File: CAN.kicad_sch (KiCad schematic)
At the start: 7 parts, among them J10 CAN, U6 LTC2875-DD

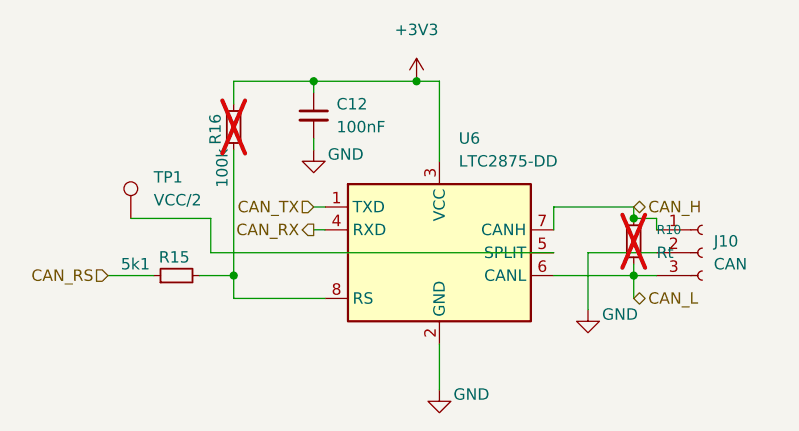
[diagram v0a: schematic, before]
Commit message: feat: more routing
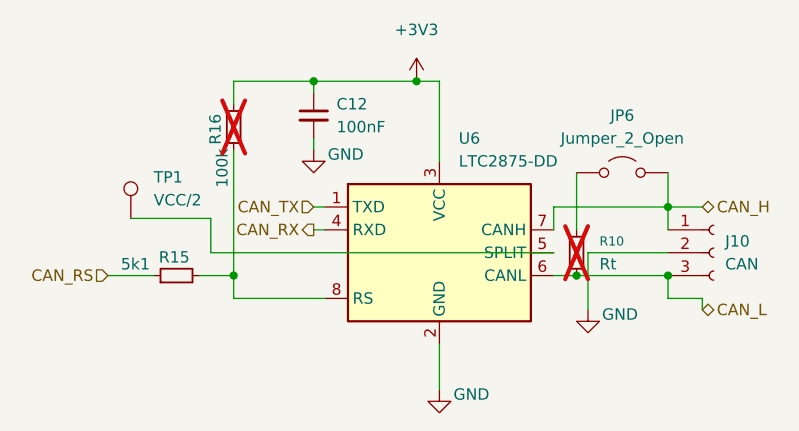
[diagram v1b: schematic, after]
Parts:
- added JP6: Jumper_2_Open, Connector_PinHeader_2.54mm:PinHeader_1x02_P2.54mm_Vertical, symbol Jumper:Jumper_2_Open
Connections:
- net CAN_H: now also JP6.2 (B); no longer R10.1
- new net: JP6.1 (A), R10.1
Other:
- moved on the sheet: J10, R10
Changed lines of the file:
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@@
 	)
 	(junction
-		(at 167.64 95.25)
+		(at 161.29 101.6)
+		(diameter 0)
+		(color 0 0 0 0)
+	)
+	(junction
+		(at 171.45 93.98)
 		(diameter 0)
 		(color 0 0 0 0)
@@
 	)
 	(junction
-		(at 167.64 101.6)
+		(at 171.45 101.6)
 		(diameter 0)
 		(color 0 0 0 0)
@@
 	(wire
 		(pts
+			(xy 171.45 93.98) (xy 175.26 93.98)
+		)
+		(stroke
+			(width 0)
+			(type default)
+		)
+	)
+	(wire
+		(pts
 			(xy 146.05 80.01) (xy 146.05 88.9)
 		)
@@
 	(wire
 		(pts
-			(xy 167.64 95.25) (xy 170.18 95.25)
+			(xy 158.75 93.98) (xy 171.45 93.98)
+		)
+		(stroke
+			(width 0)
+			(type default)
+		)
+	)
+	(wire
+		(pts
+			(xy 161.29 90.17) (xy 161.29 96.52)
 		)
 		(stroke
@@
 	(wire
 		(pts
-			(xy 167.64 101.6) (xy 170.18 101.6)
+			(xy 171.45 90.17) (xy 171.45 93.98)
 		)
 		(stroke
@@
 	(wire
 		(pts
-			(xy 158.75 101.6) (xy 167.64 101.6)
+			(xy 158.75 101.6) (xy 161.29 101.6)
 		)
 		(stroke
@@
 	(wire
 		(pts
+			(xy 175.26 104.14) (xy 171.45 104.14)
+		)
+		(stroke
+			(width 0)
+			(type default)
+		)
+	)
+	(wire
+		(pts
 			(xy 120.65 99.06) (xy 120.65 95.25)
 		)
@@
 	(wire
 		(pts
-			(xy 167.64 93.98) (xy 158.75 93.98)
-		)
-		(stroke
-			(width 0)
-			(type default)
-		)
-	)
-	(wire
-		(pts
-			(xy 167.64 93.98) (xy 167.64 95.25)
+			(xy 171.45 104.14) (xy 171.45 101.6)
 		)
 		(stroke
@@
 	(wire
 		(pts
-			(xy 170.18 99.06) (xy 162.56 99.06)
-		)
-		(stroke
-			(width 0)
-			(type default)
-		)
-	)
-	(wire
-		(pts
-			(xy 170.18 95.25) (xy 170.18 96.52)
+			(xy 171.45 99.06) (xy 162.56 99.06)
+		)
+		(stroke
+			(width 0)
+			(type default)
+		)
+	)
+	(wire
+		(pts
+			(xy 171.45 93.98) (xy 171.45 96.52)
 		)
 		(stroke
@@
 	(wire
 		(pts
-			(xy 167.64 100.33) (xy 167.64 101.6)
-		)
-		(stroke
-			(width 0)
-			(type default)
-		)
-	)
-	(wire
-		(pts
-			(xy 167.64 101.6) (xy 167.64 104.14)
+			(xy 161.29 101.6) (xy 171.45 101.6)
+		)
+		(stroke
+			(width 0)
+			(type default)
+		)
+	)
+	(wire
+		(pts
+			(xy 175.26 104.14) (xy 175.26 105.41)
 		)
 		(stroke
@@
 	(hierarchical_label "CAN_H"
 		(shape bidirectional)
-		(at 167.64 93.98 0)
+		(at 175.26 93.98 0)
 		(effects
 			(font
@@
 	(hierarchical_label "CAN_L"
 		(shape bidirectional)
-		(at 167.64 104.14 0)
+		(at 175.26 105.41 0)
 		(effects
 			(font
@@
 	(symbol
 		(lib_id "Connector:Conn_01x03_Socket")
-		(at 175.26 99.06 0)
+		(at 176.53 99.06 0)
 		(unit 1)
 		(body_style 1)
@@
 		(fields_autoplaced yes)
 		(property "Reference" "J10"
-			(at 176.53 97.7899 0)
+			(at 177.8 97.7899 0)
 			(show_name no)
 			(do_not_autoplace no)
@@
 		)
 		(property "Value" "CAN"
-			(at 176.53 100.3299 0)
+			(at 177.8 100.3299 0)
 			(show_name no)
 			(do_not_autoplace no)
@@
 		)
 		(property "Footprint" "Connector_PinHeader_2.54mm:PinHeader_1x03_P2.54mm_Vertical"
-			(at 175.26 99.06 0)
+			(at 176.53 99.06 0)
 			(hide yes)
 			(show_name no)
@@
 		)
 		(property "Datasheet" ""
-			(at 175.26 99.06 0)
+			(at 176.53 99.06 0)
 			(hide yes)
 			(show_name no)
@@
 		)
 		(property "Description" "Generic connector, single row, 01x03, script generated"
-			(at 175.26 99.06 0)
+			(at 176.53 99.06 0)
 			(hide yes)
 			(show_name no)
@@
 		(lib_name "R_Small_1")
 		(lib_id "Device:R_Small")
-		(at 167.64 97.79 0)
+		(at 161.29 99.06 0)
 		(unit 1)
 		(body_style 1)
@@
 		(fields_autoplaced yes)
 		(property "Reference" "R10"
-			(at 170.18 96.5199 0)
+			(at 163.83 97.7899 0)
 			(show_name no)
 			(do_not_autoplace no)
@@
 		)
 		(property "Value" "Rt"
-			(at 170.18 99.0599 0)
+			(at 163.83 100.3299 0)
 			(show_name no)
 			(do_not_autoplace no)
@@
 		)
 		(property "Footprint" "Resistor_SMD:R_0805_2012Metric"
-			(at 167.64 97.79 0)
+			(at 161.29 99.06 0)
 			(hide yes)
 			(show_name no)
@@
 		)
 		(property "Datasheet" ""
-			(at 167.64 97.79 0)
+			(at 161.29 99.06 0)
 			(hide yes)
 			(show_name no)
@@
 		)
 		(property "Description" "Resistor, small symbol"
-			(at 167.64 97.79 0)
+			(at 161.29 99.06 0)
 			(hide yes)
 			(show_name no)
@@
 					(unit 1)
 				)
+			)
+		)
+	)
+	(symbol
+		(lib_id "Jumper:Jumper_2_Open")
+		(at 166.37 90.17 0)
+		(unit 1)
+		(body_style 1)
+		(exclude_from_sim no)
+		(in_bom yes)
+		(on_board yes)
+		(in_pos_files yes)
+		(dnp no)
+		(fields_autoplaced yes)
+		(property "Reference" "JP6"
+			(at 166.37 83.82 0)
+			(show_name no)
+			(do_not_autoplace no)
+			(effects
+				(font
+					(size 1.27 1.27)
+				)
+			)
+		)
+		(property "Value" "Jumper_2_Open"
+			(at 166.37 86.36 0)
+			(show_name no)
+			(do_not_autoplace no)
+			(effects
+				(font
+					(size 1.27 1.27)
+				)
+			)
+		)
+		(property "Footprint" "Connector_PinHeader_2.54mm:PinHeader_1x02_P2.54mm_Vertical"
+			(at 166.37 90.17 0)
+			(hide yes)
+			(show_name no)
+			(do_not_autoplace no)
+			(effects
+				(font
+					(size 1.27 1.27)
+				)
+			)
+		)
+		(property "Datasheet" ""
+			(at 166.37 90.17 0)
+			(hide yes)
+			(show_name no)
+			(do_not_autoplace no)
+			(effects
+				(font
+					(size 1.27 1.27)
+				)
+			)
+		)
+		(property "Description" "Jumper, 2-pole, open"
+			(at 166.37 90.17 0)
+			(hide yes)
+			(show_name no)
+			(do_not_autoplace no)
+			(effects
+				(font
+					(size 1.27 1.27)
+				)
+			)
+		)
+		(pin "2"
+		)
+		(pin "1"
+		)
+		(instances
+			(project "USB-FalCAN"
+				(path "/26096f25-a87e-4f6d-a99b-624957e9ad57/1a5453f2-2452-47a2-9836-43155a3e3471"
+					(reference "JP7")
+					(unit 1)
+				)
+				(path "/26096f25-a87e-4f6d-a99b-624957e9ad57/9822f886-7d7c-4a8d-9432-f38dfb004f71"
+					(reference "JP6")
+					(unit 1)
+				)
+				(path "/26096f25-a87e-4f6d-a99b-624957e9ad57/d1b681e3-3598-4665-bb50-46c3b91c3a1a"
+					(reference "JP8")
+					(unit 1)
+				)
